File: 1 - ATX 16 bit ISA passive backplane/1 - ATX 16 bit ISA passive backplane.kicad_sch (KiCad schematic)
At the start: 22 parts, among them J1 BUS 1, J10 AB15, J11 AB15, J12 AB15, J13 AB15, J14 AB15, J15 AB15, J16 AB15, J2 BUS 2, J3 BUS 3, J4 BUS 4, J5 BUS 5, J6 BUS 6, J7 BUS 7, J8 BREADBOARD HEADER (RC2014 COM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, J9 EXTENDED HEADER

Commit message: Finally finalized the backplane to my liking.
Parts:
- removed J10, J11, J12, J13, J14, J15, J16: AB15, 0_Library:PinHeader_2x2_Vertical (Modified), symbol Connector_Generic:Conn_02x02_Odd_Even
- removed J8: BREADBOARD HEADER (RC2014 COMPATIBLE), Connector_PinHeader_2.54mm:PinHeader_1x40_P2.54mm_Vertical, symbol Connector_Generic:Conn_01x40
- removed J9: EXTENDED HEADER, Connector_PinHeader_2.54mm:PinHeader_1x22_P2.54mm_Vertical, symbol Connector_Generic:Conn_01x22
- removed LOGO1: Logo_Open_Hardware_Small, 0_Library:MicroHobbyist, symbol Graphic:Logo_Open_Hardware_Small
- removed LOGO3: Logo_Open_Hardware_Small, 0_Library:JLCPCB Logo 3, symbol Graphic:Logo_Open_Hardware_Small
- removed LOGO4, LOGO6: Logo_Open_Hardware_Small, Symbol:ESD-Logo_6.6x6mm_SilkScreen, symbol Graphic:Logo_Open_Hardware_Small
- added J2: A: Component Side, Connector_PinHeader_2.54mm:PinHeader_1x31_P2.54mm_Vertical, symbol Connector_Generic:Conn_01x31
- added J3: B: Back Side, Connector_PinHeader_2.54mm:PinHeader_1x31_P2.54mm_Vertical, symbol Connector_Generic:Conn_01x31
- renumbered J2 to J4, J3 to J5, J4 to J6, J5 to J7, J6 to J8, J7 to J9, LOGO2 to LOGO1, LOGO5 to LOGO2
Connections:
- net -5V is gone; now on net +3V3: J1.36 (B5), J4.36 (B5), J5.36 (B5), J6.36 (B5), J7.36 (B5), J8.36 (B5), J9.36 (B5)
- net IEI1 is gone; now on net ~{BUSRQ}: J1.46 (B15)
- net IEI2 is gone; now on net ~{BUSRQ}: J4.46 (B15)
- net IEI3 is gone; now on net ~{BUSRQ}: J5.46 (B15)
- net IEI4 is gone; now on net ~{BUSRQ}: J6.46 (B15)
- net IEI5 is gone; now on net ~{BUSRQ}: J7.46 (B15)
- net IEI6 is gone; now on net ~{BUSRQ}: J8.46 (B15)
- net IEI7 is gone; now on net ~{BUSRQ}: J9.46 (B15)
- net IEO1 is gone; now on net SCL: J1.15 (A15)
- net IEO2 is gone; now on net SCL: J4.15 (A15)
- net IEO3 is gone; now on net SCL: J5.15 (A15)
- net IEO4 is gone; now on net SCL: J6.15 (A15)
- net IEO5 is gone; now on net SCL: J7.15 (A15)
- net IEO6 is gone; now on net SCL: J8.15 (A15)
- net IEO7 is gone; now on net SCL: J9.15 (A15)
- net ~{INT} is gone; now on net ~{BUSAK}: J1.47 (B16), J4.47 (B16), J5.47 (B16), J6.47 (B16), J7.47 (B16), J8.47 (B16), J9.47 (B16)
- net +12V: now also J3.9 (Pin_9)
- net +3V3: now also J3.5 (Pin_5); no longer J1.50 (B19), J4.50 (B19), J5.50 (B19), J6.50 (B19), J7.50 (B19), J8.50 (B19), J9.50 (B19)
- net +5V: now also J3.29 (Pin_29), J3.3 (Pin_3)
- net -12V: now also J3.7 (Pin_7)
- net A0: now also J2.31 (Pin_31)
- net A1: now also J2.30 (Pin_30)
- net A10: now also J2.21 (Pin_21)
- net A11: now also J2.20 (Pin_20)
- net A12: now also J2.19 (Pin_19)
- net A13: now also J2.18 (Pin_18)
- net A14: now also J2.17 (Pin_17)
- net A15: now also J2.16 (Pin_16)
- net A2: now also J2.29 (Pin_29)
- net A3: now also J2.28 (Pin_28)
- net A4: now also J2.27 (Pin_27)
- net A5: now also J2.26 (Pin_26)
- net A6: now also J2.25 (Pin_25)
- net A7: now also J2.24 (Pin_24)
- net A8: now also J2.23 (Pin_23)
- net A9: now also J2.22 (Pin_22)
- net CLK: now also J3.20 (Pin_20)
- net CLK2: now also J1.39 (B8), J4.39 (B8), J5.39 (B8), J6.39 (B8), J7.39 (B8), J8.39 (B8), J9.39 (B8), J3.8 (Pin_8); no longer J1.61 (B30), J4.61 (B30), J5.61 (B30), J6.61 (B30), J7.61 (B30), J8.61 (B30), J9.61 (B30)
- net D0: now also J2.9 (Pin_9)
- net D1: now also J2.8 (Pin_8)
- net D2: now also J2.7 (Pin_7)
- net D3: now also J2.6 (Pin_6)
- net D4: now also J2.5 (Pin_5)
- net D5: now also J2.4 (Pin_4)
- net D6: now also J2.3 (Pin_3)
- net D7: now also J2.2 (Pin_2)
- net GND: now also J3.1 (Pin_1), J3.10 (Pin_10), J3.31 (Pin_31)
- net MISO: now also J1.12 (A12), J4.12 (A12), J5.12 (A12), J6.12 (A12), J7.12 (A12), J8.12 (A12), J9.12 (A12), J2.12 (Pin_12); no longer J1.13 (A13), J4.13 (A13), J5.13 (A13), J6.13 (A13), J7.13 (A13), J8.13 (A13), J9.13 (A13)
- net MOSI: now also J1.11 (A11), J4.11 (A11), J5.11 (A11), J6.11 (A11), J7.11 (A11), J8.11 (A11), J9.11 (A11), J2.11 (Pin_11); no longer J1.14 (A14), J4.14 (A14), J5.14 (A14), J6.14 (A14), J7.14 (A14), J8.14 (A14), J9.14 (A14)
- net RX: now also J1.10 (A10), J4.10 (A10), J5.10 (A10), J6.10 (A10), J7.10 (A10), J8.10 (A10), J9.10 (A10), J2.10 (Pin_10); no longer J1.11 (A11), J4.11 (A11), J5.11 (A11), J6.11 (A11), J7.11 (A11), J8.11 (A11), J9.11 (A11)
- net SCL: now also J2.15 (Pin_15); no longer J1.1 (A1), J4.1 (A1), J5.1 (A1), J6.1 (A1), J7.1 (A1), J8.1 (A1), J9.1 (A1)
- net SCLK: now also J1.13 (A13), J4.13 (A13), J5.13 (A13), J6.13 (A13), J7.13 (A13), J8.13 (A13), J9.13 (A13), J2.13 (Pin_13); no longer J1.12 (A12), J4.12 (A12), J5.12 (A12), J6.12 (A12), J7.12 (A12), J8.12 (A12), J9.12 (A12)
- net SDA: now also J1.14 (A14), J4.14 (A14), J5.14 (A14), J6.14 (A14), J7.14 (A14), J8.14 (A14), J9.14 (A14), J2.14 (Pin_14); no longer J1.35 (B4), J4.35 (B4), J5.35 (B4), J6.35 (B4), J7.35 (B4), J8.35 (B4), J9.35 (B4)
- net TX: now also J1.1 (A1), J4.1 (A1), J5.1 (A1), J6.1 (A1), J7.1 (A1), J8.1 (A1), J9.1 (A1), J2.1 (Pin_1); no longer J1.10 (A10), J4.10 (A10), J5.10 (A10), J6.10 (A10), J7.10 (A10), J8.10 (A10), J9.10 (A10)
- net ~{BUSAK}: now also J3.16 (Pin_16); no longer J1.48 (B17), J4.48 (B17), J5.48 (B17), J6.48 (B17), J7.48 (B17), J8.48 (B17), J9.48 (B17)
- net ~{BUSRQ}: now also J3.15 (Pin_15); no longer J1.49 (B18), J4.49 (B18), J5.49 (B18), J6.49 (B18), J7.49 (B18), J8.49 (B18), J9.49 (B18)
- net ~{CLK}: now also J1.61 (B30), J4.61 (B30), J5.61 (B30), J6.61 (B30), J7.61 (B30), J8.61 (B30), J9.61 (B30), J3.30 (Pin_30); no longer J1.58 (B27), J4.58 (B27), J5.58 (B27), J6.58 (B27), J7.58 (B27), J8.58 (B27), J9.58 (B27)
- net ~{HALT}: now also J1.49 (B18), J4.49 (B18), J5.49 (B18), J6.49 (B18), J7.49 (B18), J8.49 (B18), J9.49 (B18), J3.18 (Pin_18); no longer J1.57 (B26), J4.57 (B26), J5.57 (B26), J6.57 (B26), J7.57 (B26), J8.57 (B26), J9.57 (B26)
- net ~{IORQ}: now also J3.12 (Pin_12)
- net ~{IRQ3}: now also J3.25 (Pin_25)
- net ~{IRQ4}: now also J3.24 (Pin_24)
- net ~{IRQ5}: now also J3.23 (Pin_23)
- net ~{IRQ6}: now also J3.22 (Pin_22)
- net ~{IRQ7}: now also J3.21 (Pin_21)
- net ~{M1}: now also J1.37 (B6), J4.37 (B6), J5.37 (B6), J6.37 (B6), J7.37 (B6), J8.37 (B6), J9.37 (B6), J3.6 (Pin_6); no longer J1.59 (B28), J4.59 (B28), J5.59 (B28), J6.59 (B28), J7.59 (B28), J8.59 (B28), J9.59 (B28)
- net ~{MREQ}: now also J3.11 (Pin_11)
- net ~{NMI}: now also J1.57 (B26), J4.57 (B26), J5.57 (B26), J6.57 (B26), J7.57 (B26), J8.57 (B26), J9.57 (B26), J3.26 (Pin_26); no longer J1.37 (B6), J4.37 (B6), J5.37 (B6), J6.37 (B6), J7.37 (B6), J8.37 (B6), J9.37 (B6)
- net ~{RD}: now also J3.14 (Pin_14)
- net ~{RESET}: now also J3.2 (Pin_2)
- net ~{WAIT}: now also J1.48 (B17), J4.48 (B17), J5.48 (B17), J6.48 (B17), J7.48 (B17), J8.48 (B17), J9.48 (B17), J3.17 (Pin_17); no longer J1.39 (B8), J4.39 (B8), J5.39 (B8), J6.39 (B8), J7.39 (B8), J8.39 (B8), J9.39 (B8)
- net ~{WR}: now also J3.13 (Pin_13)
- new net CTCLK1: J1.58 (B27), J3.27 (Pin_27), J4.58 (B27), J5.58 (B27), J6.58 (B27), J7.58 (B27), J8.58 (B27), J9.58 (B27)
- new net CTCLK2: J1.59 (B28), J3.28 (Pin_28), J4.59 (B28), J5.59 (B28), J6.59 (B28), J7.59 (B28), J8.59 (B28), J9.59 (B28)
- new net ~{IRQ2}: J1.35 (B4), J3.4 (Pin_4), J4.35 (B4), J5.35 (B4), J6.35 (B4), J7.35 (B4), J8.35 (B4), J9.35 (B4)
- new net ~{RFSH}: J1.50 (B19), J3.19 (Pin_19), J4.50 (B19), J5.50 (B19), J6.50 (B19), J7.50 (B19), J8.50 (B19), J9.50 (B19)
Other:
- sheet Reset & LEDs ports: added A7; removed none
- note added: "Suggested IRQ levels: --------------------- IRQ 0 * System Timer (CTC) IRQ 1 * COM1 & COM2 (SIO) IRQ 2 * Keyboard (PS/2) IRQ 3 * VDP IRQ 4 * Real Time Clock IRQ 5 * Additional SIOs (Shared IRQ) IRQ 6 * PIOs and other devices IRQ 7 * Mouse (PS/2)"
- note removed: "*"
- note removed: "AB15 are bypass jumbers. When installed horizontally (2-4 and 1-3), acts as a standard bus line. When installed verticaly (1-2 or 3-4), determines the direction of IEI and IEO for Z80 mode 2 interrupts."
- note removed: "B19, normally associated with ~{REFRESH} on x86, has been reassigned to +3.3V. There is a bypass jumper to do away with +3.3V rail, and convert it back to a standard bus lane."
- note removed: "FRE80 IRQ 0 * System Timer (CTC IRQ 1 * PS/2 Keyboard IRQ 2 * COM 1 & 2 IRQ 8 * Real Time Clock IRQ 9 * PS/2 Mouse"
- note removed: "PC IRQ LIST IRQ 0 System Timer IRQ 1 Keyboard IRQ 2 Cascaded with IRQ 9 IRQ 3 Default COM2 and COM4 IRQ 4 Default COM1 and COM3 IRQ 5 LPT2 IRQ 6 Floppy Drive Controller IRQ 7 LPT1 IRQ 8 Real Time Clock IRQ 9 SEE 2 IRQ 10 Open IRQ 11 Open IRQ 12 PS/2 mouse or Open IRQ 13 Math Coprocessor IRQ 14 Primary Hard Drive controller IRQ 15 Secondary Hard Drive controller"

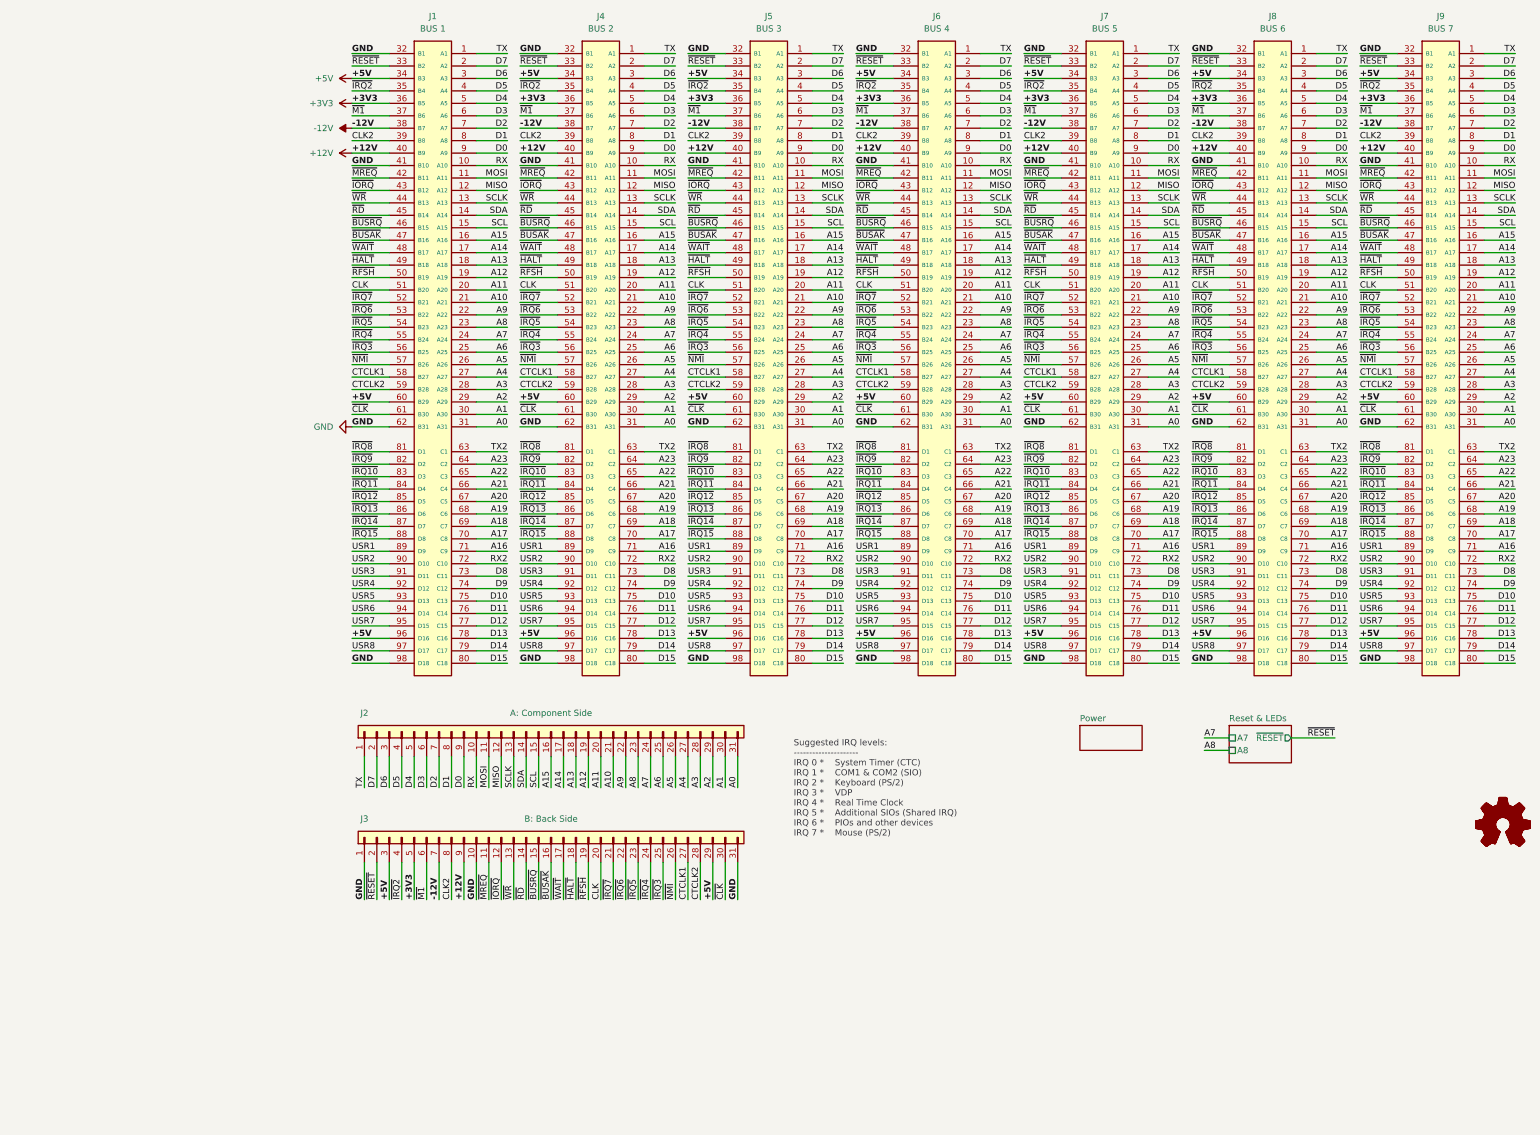
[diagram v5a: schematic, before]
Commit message: Added Interrupt Enable daisy chain jumpers between the ISA slots
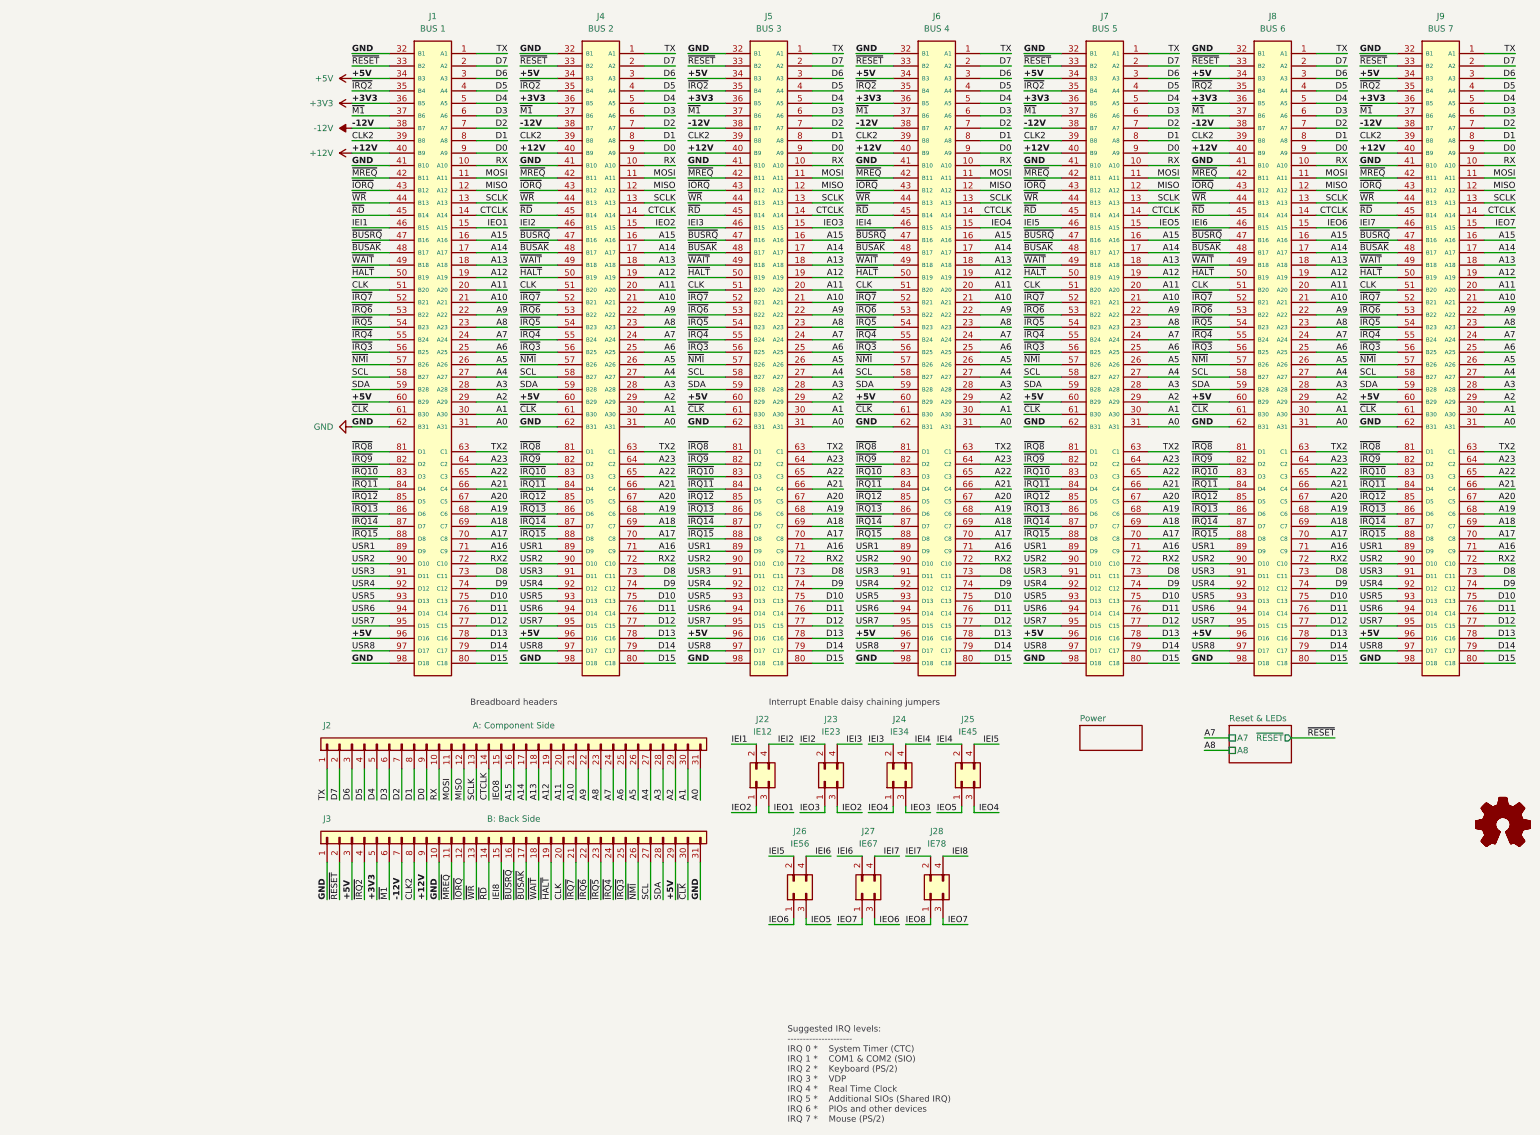
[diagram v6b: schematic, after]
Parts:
- added J22: IE12, 0_Library:PinHeader_2x2_Vertical (Modified), symbol Connector_Generic:Conn_02x02_Odd_Even
- added J23: IE23, 0_Library:PinHeader_2x2_Vertical (Modified), symbol Connector_Generic:Conn_02x02_Odd_Even
- added J24: IE34, 0_Library:PinHeader_2x2_Vertical (Modified), symbol Connector_Generic:Conn_02x02_Odd_Even
- added J25: IE45, 0_Library:PinHeader_2x2_Vertical (Modified), symbol Connector_Generic:Conn_02x02_Odd_Even
- added J26: IE56, 0_Library:PinHeader_2x2_Vertical (Modified), symbol Connector_Generic:Conn_02x02_Odd_Even
- added J27: IE67, 0_Library:PinHeader_2x2_Vertical (Modified), symbol Connector_Generic:Conn_02x02_Odd_Even
- added J28: IE78, 0_Library:PinHeader_2x2_Vertical (Modified), symbol Connector_Generic:Conn_02x02_Odd_Even
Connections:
- net CTCLK1 is gone; now on net SCL: J1.58 (B27), J3.27 (Pin_27), J4.58 (B27), J5.58 (B27), J6.58 (B27), J7.58 (B27), J8.58 (B27), J9.58 (B27)
- net CTCLK2 is gone; now on net SDA: J1.59 (B28), J3.28 (Pin_28), J4.59 (B28), J5.59 (B28), J6.59 (B28), J7.59 (B28), J8.59 (B28), J9.59 (B28)
- net ~{RFSH} is gone; now on net ~{HALT}: J1.50 (B19), J3.19 (Pin_19), J4.50 (B19), J5.50 (B19), J6.50 (B19), J7.50 (B19), J8.50 (B19), J9.50 (B19)
- net SCL: no longer J1.15 (A15), J2.15 (Pin_15), J4.15 (A15), J5.15 (A15), J6.15 (A15), J7.15 (A15), J8.15 (A15), J9.15 (A15)
- net SDA: no longer J1.14 (A14), J2.14 (Pin_14), J4.14 (A14), J5.14 (A14), J6.14 (A14), J7.14 (A14), J8.14 (A14), J9.14 (A14)
- net ~{BUSAK}: now also J1.48 (B17), J3.17 (Pin_17), J4.48 (B17), J5.48 (B17), J6.48 (B17), J7.48 (B17), J8.48 (B17), J9.48 (B17); no longer J1.47 (B16), J3.16 (Pin_16), J4.47 (B16), J5.47 (B16), J6.47 (B16), J7.47 (B16), J8.47 (B16), J9.47 (B16)
- net ~{BUSRQ}: now also J1.47 (B16), J3.16 (Pin_16), J4.47 (B16), J5.47 (B16), J6.47 (B16), J7.47 (B16), J8.47 (B16), J9.47 (B16); no longer J1.46 (B15), J3.15 (Pin_15), J4.46 (B15), J5.46 (B15), J6.46 (B15), J7.46 (B15), J8.46 (B15), J9.46 (B15)
- net ~{HALT}: no longer J1.49 (B18), J3.18 (Pin_18), J4.49 (B18), J5.49 (B18), J6.49 (B18), J7.49 (B18), J8.49 (B18), J9.49 (B18)
- net ~{WAIT}: now also J1.49 (B18), J3.18 (Pin_18), J4.49 (B18), J5.49 (B18), J6.49 (B18), J7.49 (B18), J8.49 (B18), J9.49 (B18); no longer J1.48 (B17), J3.17 (Pin_17), J4.48 (B17), J5.48 (B17), J6.48 (B17), J7.48 (B17), J8.48 (B17), J9.48 (B17)
- new net CTCLK: J1.14 (A14), J2.14 (Pin_14), J4.14 (A14), J5.14 (A14), J6.14 (A14), J7.14 (A14), J8.14 (A14), J9.14 (A14)
- new net IEI1: J1.46 (B15), J22.2 (Pin_2)
- new net IEI2: J22.4 (Pin_4), J23.2 (Pin_2), J4.46 (B15)
- new net IEI3: J23.4 (Pin_4), J24.2 (Pin_2), J5.46 (B15)
- new net IEI4: J24.4 (Pin_4), J25.2 (Pin_2), J6.46 (B15)
- new net IEI5: J25.4 (Pin_4), J26.2 (Pin_2), J7.46 (B15)
- new net IEI6: J26.4 (Pin_4), J27.2 (Pin_2), J8.46 (B15)
- new net IEI7: J27.4 (Pin_4), J28.2 (Pin_2), J9.46 (B15)
- new net IEI8: J28.4 (Pin_4), J3.15 (Pin_15)
- new net IEO1: J1.15 (A15), J22.3 (Pin_3)
- new net IEO2: J22.1 (Pin_1), J23.3 (Pin_3), J4.15 (A15)
- new net IEO3: J23.1 (Pin_1), J24.3 (Pin_3), J5.15 (A15)
- new net IEO4: J24.1 (Pin_1), J25.3 (Pin_3), J6.15 (A15)
- new net IEO5: J25.1 (Pin_1), J26.3 (Pin_3), J7.15 (A15)
- new net IEO6: J26.1 (Pin_1), J27.3 (Pin_3), J8.15 (A15)
- new net IEO7: J27.1 (Pin_1), J28.3 (Pin_3), J9.15 (A15)
- new net IEO8: J2.15 (Pin_15), J28.1 (Pin_1)
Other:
- note added: "Breadboard headers"
- note added: "Interrupt Enable daisy chaining jumpers"
- moved on the sheet: J2, J3

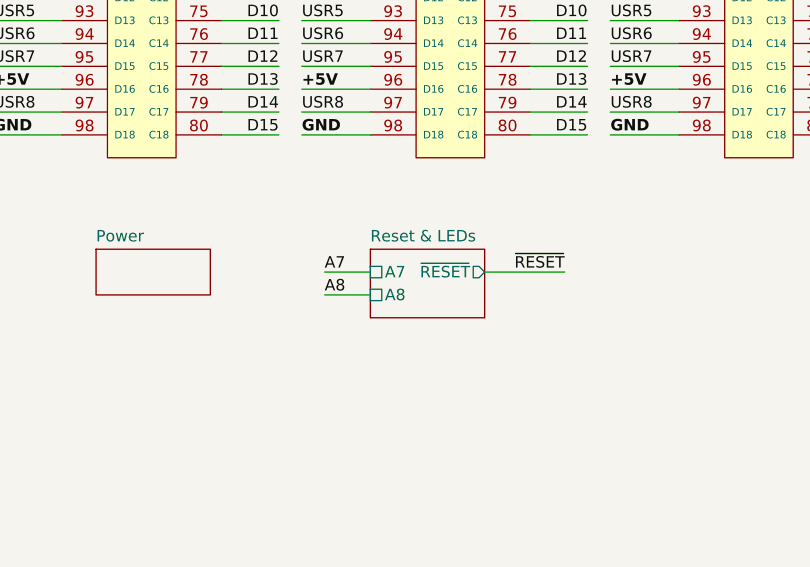
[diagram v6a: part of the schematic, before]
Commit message: Removed the alternate power input.
The soft power on circuit was flaky upon testing.
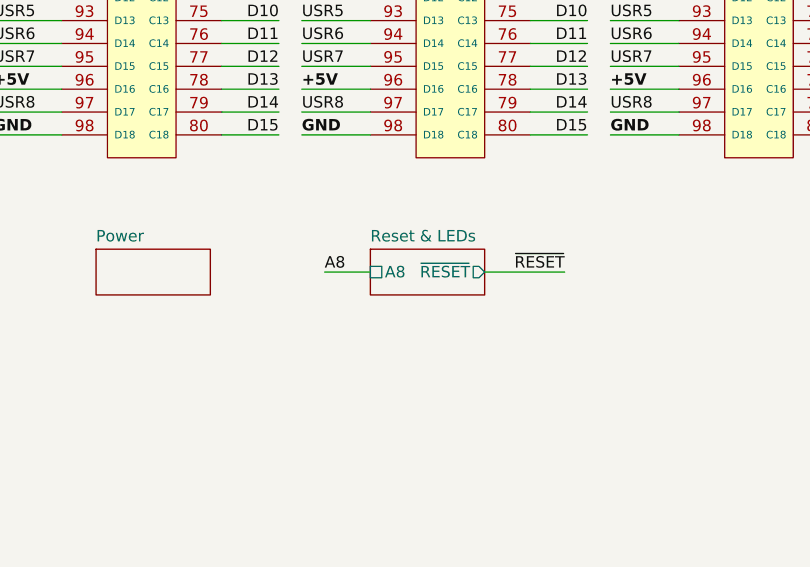
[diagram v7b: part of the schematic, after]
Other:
- sheet Reset & LEDs ports: added none; removed A7
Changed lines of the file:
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@@
   (title_block
     (title "7-slot 16-bit ATX backblane with breadboard connectivity")
-    (date "2023-08-21")
+    (date "2023-09-02")
     (rev "2.1")
     (company "Frederic Segard  (@microhobbyist)")
@@
     (stroke (width 0) (type default))
   )
-  (wire (pts (xy 198.12 162.56) (xy 203.2 162.56))
-    (stroke (width 0) (type default))
-  )
   (wire (pts (xy 120.65 177.8) (xy 120.65 176.53))
     (stroke (width 0) (type default))
@@
     (stroke (width 0) (type default))
   )
-  (wire (pts (xy 198.12 165.1) (xy 203.2 165.1))
+  (wire (pts (xy 198.12 162.56) (xy 203.2 162.56))
     (stroke (width 0) (type default))
   )
@@
     (effects (font (size 1.27 1.27)) (justify left bottom))
   )
-  (label "A7" (at 198.12 162.56 0) (fields_autoplaced)
-    (effects (font (size 1.27 1.27)) (justify left bottom))
-  )
   (label "A21" (at 227.33 111.76 180) (fields_autoplaced)
     (effects (font (size 1.27 1.27)) (justify right bottom))
@@
     (effects (font (size 1.27 1.27)) (justify left bottom))
   )
-  (label "A8" (at 198.12 165.1 0) (fields_autoplaced)
+  (label "A8" (at 198.12 162.56 0) (fields_autoplaced)
     (effects (font (size 1.27 1.27)) (justify left bottom))
   )
@@
     )
   )
-  (sheet (at 203.2 160.02) (size 12.7 7.62) (fields_autoplaced)
+  (sheet (at 203.2 160.02) (size 12.7 5.08) (fields_autoplaced)
     (stroke (width 0.1524) (type solid))
     (fill (color 0 0 0 0.0000))
@@
       (effects (font (size 1.27 1.27)) (justify left bottom))
     )
-    (property "Sheetfile" "ResetCircuit.kicad_sch" (at 203.2 168.2246 0)
+    (property "Sheetfile" "ResetCircuit.kicad_sch" (at 203.2 165.6846 0)
       (effects (font (size 1.27 1.27)) (justify left top) hide)
     )
@@
       (effects (font (size 1.27 1.27)) (justify right))
     )
-    (pin "A8" passive (at 203.2 165.1 180)
-      (effects (font (size 1.27 1.27)) (justify left))
-    )
-    (pin "A7" passive (at 203.2 162.56 180)
+    (pin "A8" passive (at 203.2 162.56 180)
       (effects (font (size 1.27 1.27)) (justify left))
     )
